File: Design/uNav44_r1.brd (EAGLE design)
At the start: 39.6 x 39.6 mm, 36 parts, among them IC1 DSPIC33FJ128MC, IC2 24LC024, Q1 10MHz

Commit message: Add 5 and 3.3V regulator / @katodo you must verify
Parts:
- removed PS: (no value), Personale:2POL254
- removed VR1: MCP1754S-3.3V, Personale:SOT89
- added C11, C13: 22uf, rcl:C1206
- added C12: 100nF/S, rcl:C0603
- added C14, C15: 10nF/S, rcl:C0603
- added IC3: (no value), OfficineRobotiche:SOT-23-5
- added IC4: (no value), OfficineRobotiche:SO-8EP
- added L2, L3: 22 uH, SparkFun-Passives:0805
- added PS1: (no value), Personale:2POL254
- added R10, R12: 10K0/S 1%, rcl:R0603
- added R11: 45K3/S 1%, rcl:R0603
- added R9: 100K0/S 1%, rcl:R0603
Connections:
- new net N$1: IC3.3, L3.1
- new net N$15: C14.2, IC4.3, L2.1
- new net N$16: C15.1, IC4.6
- new net N$17: C15.2, R12.2
- new net N$4: C14.1, IC4.1
- new net N$6: IC4.7, R9.1
- new net N$8: C12.1, IC4.8
- new net N$9: IC4.5, R10.1, R11.1
- net +12V: now also C11.1, IC4.2, PS1.2, R9.2
- net +3V3: now also IC3.5, L3.2; no longer VR1.3
- net +5V: now also C13.1, IC3.1, IC3.4, L2.2, R11.2; no longer PS.1, VR1.1
- net GND: now also C11.2, C12.2, C13.2, IC3.2, IC4.4, IC4.PAD, PS1.1, R10.2, R12.1; no longer PS.2, VR1.2, VR1.4
- net VENC: now also SJ3.2
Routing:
- net GND: track 279.7 -> 273.1 mm
- net +5V: track 61.7 -> 59.4 mm

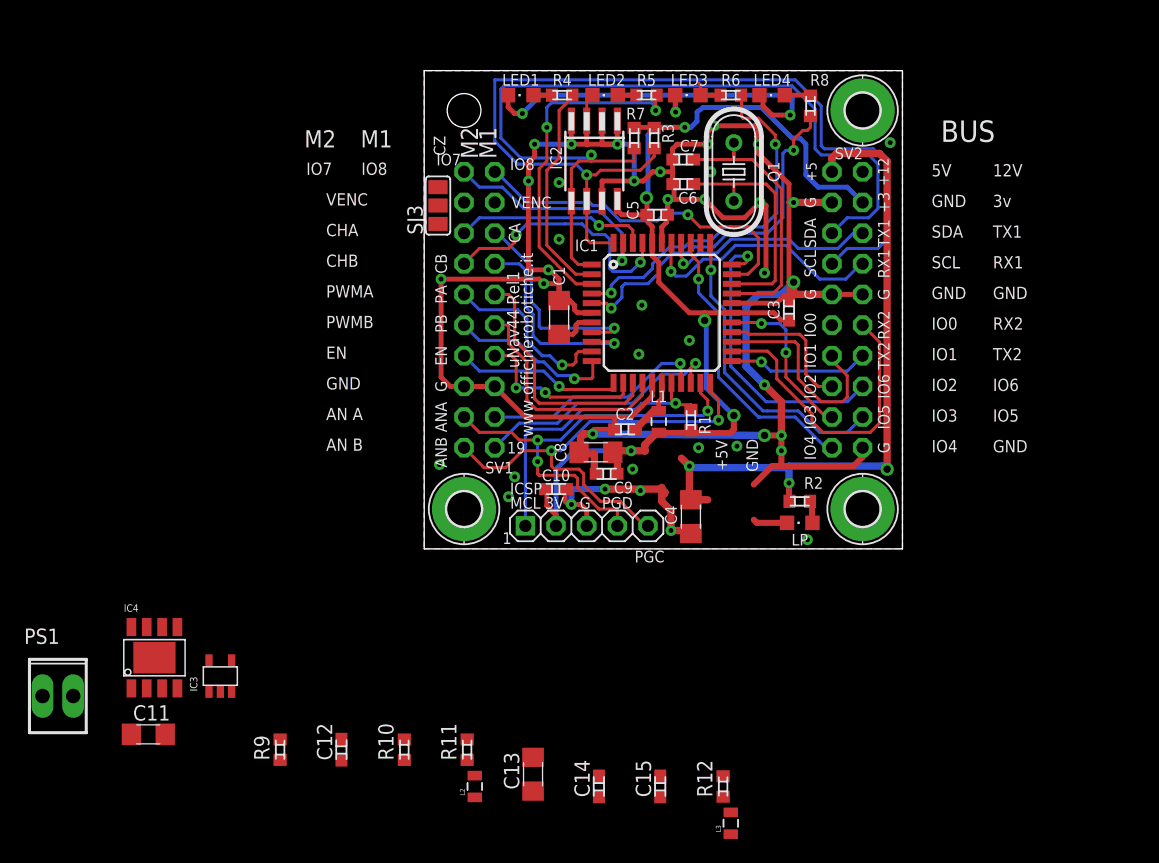
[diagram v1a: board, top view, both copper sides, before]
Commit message: Changed some component package to optimize space.
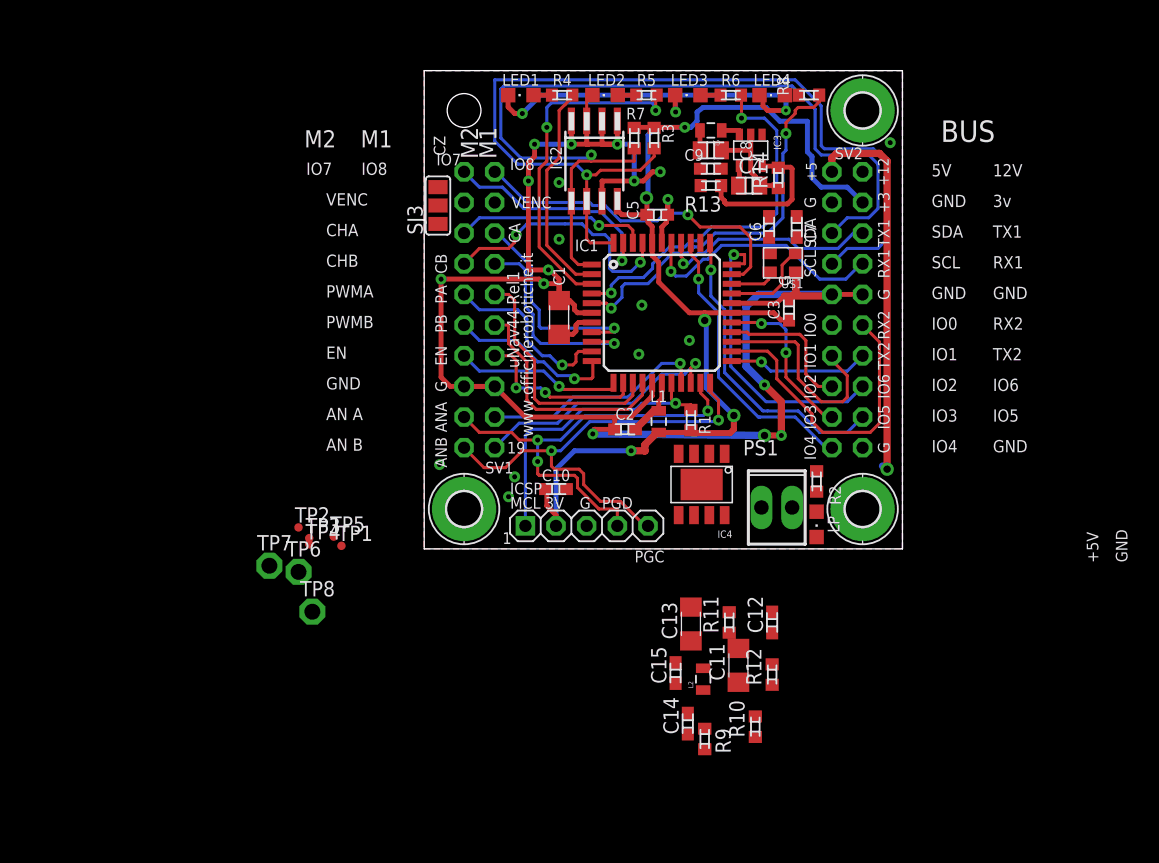
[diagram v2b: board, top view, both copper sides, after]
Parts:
- removed Q1: 10MHz, crystal:HC49U-V
- added R13: 450K/S 1%, rcl:R0603
- added R14: 100K/S 1%, rcl:R0603
- added TP1, TP2, TP3, TP4, TP5: PTR1TP07R, testpad:TP07R
- added TP6, TP7, TP8: PTR1PAD1-13, testpad:P1-13
- added U$1: CTS_32X25_SMD, cts_crystal:CTS_32X25
- C4, C8: value 22uf -> 10uF 10V X7R; device rcl:C1206 -> rcl:C0805
- IC3: value (none) -> AP3417CK-3.3TRG1
- IC4: value (none) -> AP6503SP-13
- L3: value 22 uH -> ASMPH-0805-2R2M-T
- moved IC3 61.9 mm to (23.7, 29.7), turned to 180 degrees
- moved PS1 61.6 mm to (25.9, 0.13)
- moved L3 57.4 mm to (20.4, 31.4), turned to 180 degrees
- moved C11 49.2 mm to (22.7, -13.0), turned to 90 degrees
- moved IC4 47.6 mm to (19.7, 2.03), turned to 180 degrees
- moved C12 37.2 mm to (25.5, -9.40)
- moved R9 35.2 mm to (19.9, -19.1), turned to 270 degrees
- moved R10 29.1 mm to (24.1, -18.0)
- moved C4 27.9 mm to (23.6, 26.8), turned to 0 degrees
- moved C8 26.8 mm to (20.4, 29.7), turned to 0 degrees
- moved C9 26.7 mm to (20.4, 28.2), turned to 0 degrees
- moved R11 24.1 mm to (22.0, -9.40)
- moved L2 20.9 mm to (19.8, -14.1)
- moved C13 18.1 mm to (18.8, -9.53)
- moved C7 10.9 mm to (27.6, 23.4), turned to 270 degrees
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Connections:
- new net N$7: IC3.5, R13.1, R14.2
- net +3V3: now also R13.2, TP1.TP; no longer IC3.5
- net +5V: now also TP2.TP
- net GND: now also R14.1, TP6.TP, TP7.TP, TP8.TP, U$1.2, U$1.4
- net N$2: now also U$1.1; no longer Q1.1
- net N$3: now also U$1.3; no longer Q1.2
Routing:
- net GND: track 273.1 -> 189.6 mm, vias 44 -> 26
- net +5V: track 59.4 -> 33.7 mm, vias 3 -> 1
- net N$2: track 23.4 -> 7.61 mm
- net N$3: track 19.4 -> 3.83 mm
- net N$7: track 0.00 -> 12.5 mm
- net VENC2-LD4: track 2.61 -> 0.35 mm
- net LD4: track 29.9 -> 32.1 mm
- net N$5: track 1.98 -> 0.00 mm
- net N$1: track 0.00 -> 1.81 mm
- net IO8: track 29.3 -> 28.2 mm
- net VENC1-LD3: track 2.74 -> 1.66 mm
- net +3V3: track 98.2 -> 97.2 mm
- net LD3: track 30.6 -> 31.1 mm

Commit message: Scheme update with Operational Amplifier and switching supply
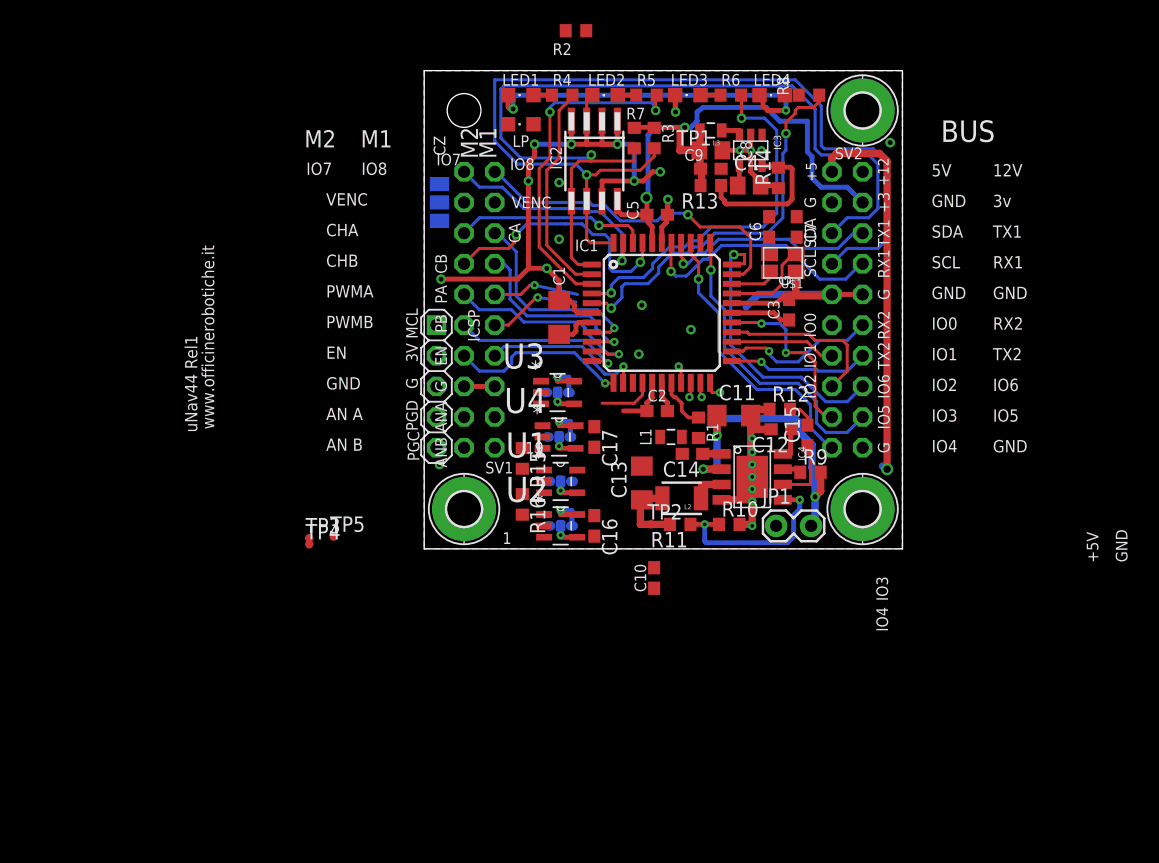
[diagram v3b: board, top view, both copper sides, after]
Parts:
- removed PS1: (no value), Personale:2POL254
- removed TP6, TP7, TP8: PTR1PAD1-13, testpad:P1-13
- added C16, C17: 100nF/S, rcl:C0603
- added JMP1, JMP2, JMP3, JMP4: 0R-JUMPC, jump-0r-smd:C0R-JMP
- added JP1: M02LOCK, SparkFun-Connectors:1X02_LOCK
- added R15, R16: 10K0/S 1%, rcl:R0603
- added U1, U2, U3, U4: MCP6G01T-E/OT, OfficineRobotiche:SOT95P300X145-5N
- C11: value 22uf -> 22uF 35V 20% JB 1206
- C12: value 100nF/S -> 100nF/S2
- C15: value 10nF/S -> 10nF/S2
- L2: value 22 uH -> 10uH_520mA; device SparkFun-Passives:0805 -> SparkFun-Passives:1210
- R9: value 100K0/S 1% -> 100K0/S2 1%
- U$1: value CTS_32X25_SMD -> (none); device cts_crystal:CTS_32X25 -> OfficineRobotiche:CTS_32X25
- moved TP1 43.1 mm to (17.9, 29.7)
- moved R2 42.3 mm to (9.27, 39.6), turned to 0 degrees
- moved LP 41.2 mm to (4.70, 31.9), turned to 90 degrees
- moved TP2 29.2 mm to (15.5, -1.27)
- moved R9 23.8 mm to (28.7, 3.05), turned to 0 degrees
- moved C15 22.5 mm to (28.4, 6.10)
- moved C14 22.4 mm to (18.9, 4.57), turned to 180 degrees
- moved R12 22.0 mm to (26.2, 8.26), turned to 0 degrees
- moved C11 20.7 mm to (22.4, 7.75), turned to 0 degrees
- moved ICSP 17.0 mm to (-2.29, 10.2), turned to 270 degrees
- moved R10 16.9 mm to (22.0, -1.27), turned to 0 degrees
- moved C12 16.0 mm to (26.3, 6.60), turned to 180 degrees
- moved L2 15.1 mm to (18.0, 0.89), turned to 180 degrees
- moved C13 12.4 mm to (14.7, 2.16)
- moved C10 11.0 mm to (15.7, -5.71), turned to 90 degrees
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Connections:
- new net ANA2/PGD: IC1.21, ICSP.4, R15.1
- new net ANB2/PGC: IC1.22, ICSP.5, R16.1
- new net IN_A1: SV1.17, U3.3
- new net IN_B1: SV1.19, U4.3
- new net N$11: JMP1.2, U1.4
- new net N$18: JMP2.2, U2.4
- new net N$19: JMP3.2, U3.4
- new net N$20: JMP4.2, U4.4
- new net N$21: R15.2, U1.1
- new net N$22: R16.2, U2.1
- net +12V: now also JP1.2; no longer PS1.2
- net +3V3: now also C16.1, C17.1, JMP1.1, JMP2.1, JMP3.1, JMP4.1, U1.5, U2.5, U3.5, U4.5
- net ANA1: now also U3.1; no longer SV1.17
- net ANA2: now also U1.3; no longer IC1.21, ICSP.4
- net ANB1: now also U4.1; no longer SV1.19
- net ANB2: now also U2.3; no longer IC1.22, ICSP.5
- net GND: now also C16.2, C17.2, JMP1.3, JMP2.3, JMP3.3, JMP4.3, JP1.1, U1.2, U2.2, U3.2, U4.2; no longer PS1.1, TP6.TP, TP7.TP, TP8.TP
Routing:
- net ANB2: track 38.7 -> 0.00 mm, vias 2 -> 0
- net ANA2: track 37.0 -> 0.00 mm, vias 3 -> 0
- net GND: track 189.6 -> 153.3 mm, vias 26 -> 29
- net +3V3: track 97.2 -> 70.2 mm
- net +12V: track 0.00 -> 26.7 mm, vias 0 -> 3
- net MCLR: track 24.6 -> 4.38 mm, vias 1 -> 0
- net ANB1: track 21.3 -> 1.29 mm
- net ANA1: track 18.8 -> 1.44 mm
- net N$9: track 0.00 -> 16.0 mm, vias 0 -> 2
- net PWMA1: track 20.3 -> 7.25 mm, vias 0 -> 1
- net RX2: track 25.3 -> 12.9 mm, vias 0 -> 1
- net IO1: track 17.4 -> 8.78 mm
- net PWMB1: track 19.4 -> 12.3 mm, vias 0 -> 1
- net +5V: track 33.7 -> 40.1 mm
- net N$16: track 0.00 -> 5.75 mm
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
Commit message: Work in progress... update image of layout
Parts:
- added C18, C19: 100nF/S, rcl:C0603
- moved C10 23.7 mm to (4.95, 15.4)
- moved R2 13.1 mm to (0.13, 30.2), turned to 180 degrees
- moved C6 3.29 mm to (23.7, 20.4)
- moved JMP3 2.07 mm to (6.22, 11.0)
- moved U3 2.07 mm to (6.22, 11.0)
- moved C7 1.55 mm to (26.3, 22.5), turned to 0 degrees
- moved TP2 1.53 mm to (14.0, -1.40)
- moved L1 1.31 mm to (16.0, 6.60), turned to 180 degrees
- moved R11 1.14 mm to (17.9, -2.41)
- moved L3 0.89 mm to (20.4, 32.3)
- moved C13 0.76 mm to (14.0, 2.16)
- moved C4 0.51 mm to (23.6, 26.3)
- moved TP1 0.51 mm to (17.4, 29.7)
- moved R14 0.40 mm to (26.2, 27.1)
- moved C5 0.38 mm to (16.0, 24.8)
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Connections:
- net +3V3: now also C18.1, C19.1
- net GND: now also C18.2, C19.2
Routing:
- net +3V3: track 70.2 -> 151.4 mm, vias 5 -> 10
- net GND: track 153.3 -> 233.2 mm, vias 29 -> 38
- net +5V: track 40.1 -> 117.2 mm, vias 1 -> 6
- net ANB2/PGC: track 1.52 -> 37.9 mm, vias 1 -> 4
- net +12V: track 26.7 -> 57.7 mm, vias 3 -> 4
- net ANA2/PGD: track 1.27 -> 29.0 mm, vias 1 -> 2
- net ANA1: track 1.44 -> 20.7 mm, vias 1 -> 2
- net ANB1: track 1.29 -> 18.8 mm, vias 1 -> 2
- net MCLR: track 4.38 -> 21.2 mm
- net ANB2: track 0.00 -> 12.5 mm
- net ANA2: track 0.00 -> 12.2 mm, vias 0 -> 2
- net PWMA1: track 7.25 -> 17.8 mm, vias 1 -> 2
- net N$5: track 0.00 -> 6.18 mm
- net IN_B1: track 0.00 -> 5.27 mm
- net PWMB1: track 12.3 -> 16.9 mm
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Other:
- board size 39.6 x 39.6 mm -> 39.9 x 39.9 mm

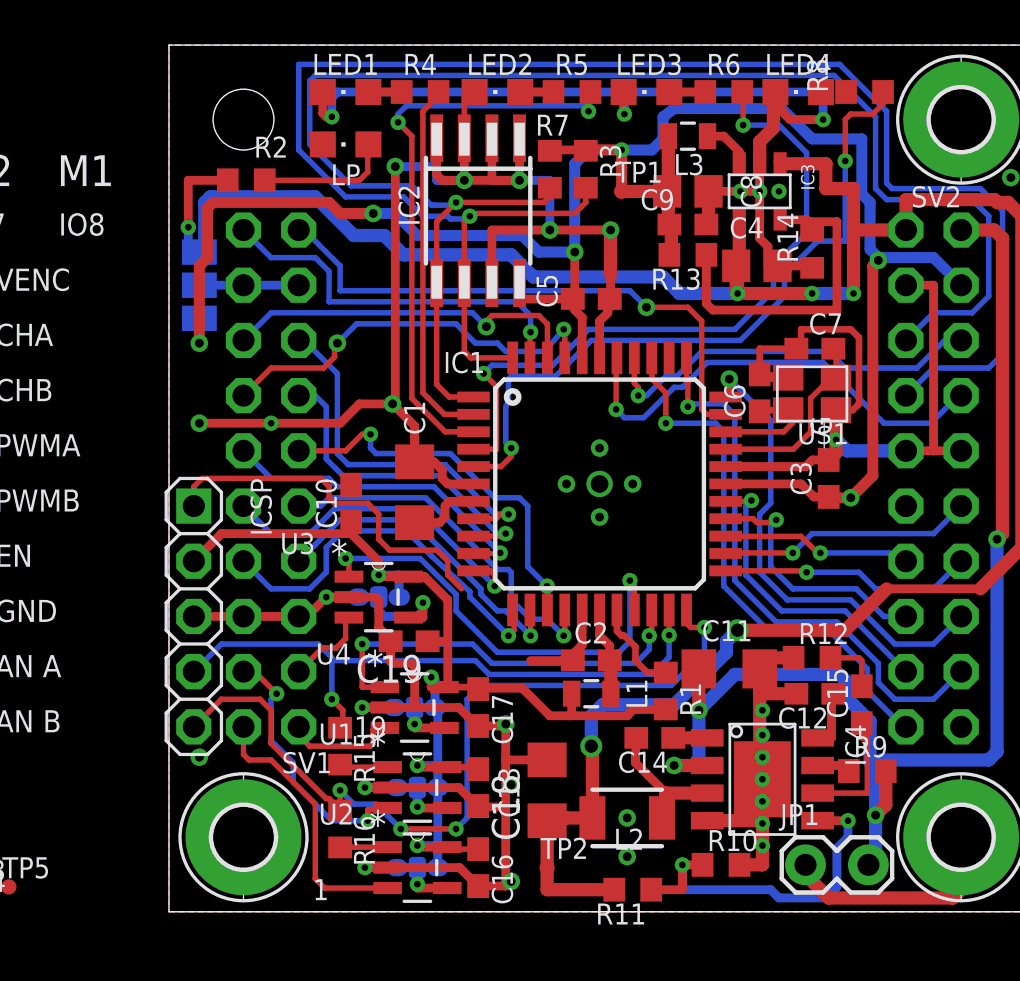
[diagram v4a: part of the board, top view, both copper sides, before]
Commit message: Re-Added LDO regulator as option for a LOW-COST version of board. Added jumper to fix IO7 & IO8 to GND to facilitate Encoder cabling in application without Z-Axis
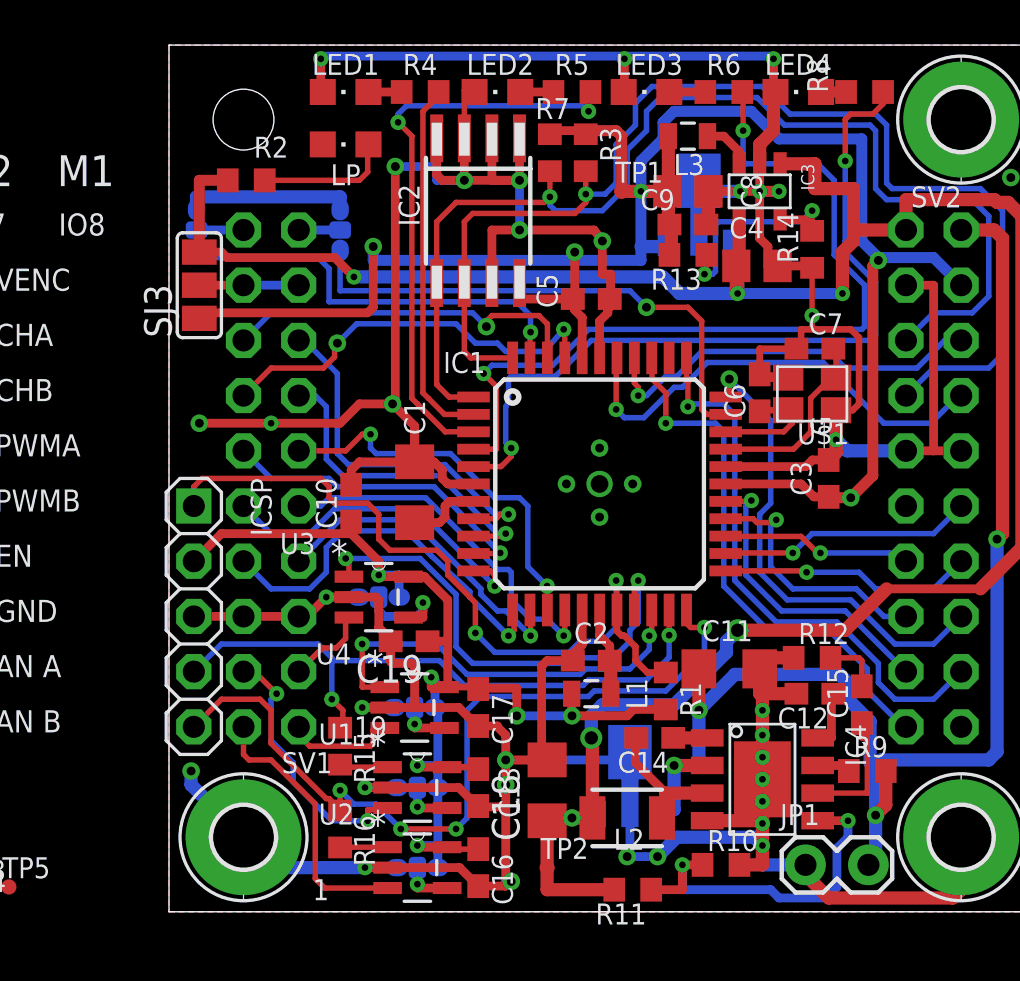
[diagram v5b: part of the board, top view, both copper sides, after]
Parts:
- added JMP5, JMP6: 0R-JUMPC, jump-0r-smd:C0R-JMP
- added VR1: MCP1754S-3.3V, Personale:SOT89
- added VR2: MCP1754S-5.0V, Personale:SOT89
- moved R3 0.76 mm to (15.7, 31.5)
- moved R7 0.76 mm to (14.1, 31.5)
- flipped SJ3 to the top
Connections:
- new net N$10: JMP5.2, SV1.2
- new net N$23: JMP6.2, SV1.1
- net +12V: now also VR2.1
- net +3V3: now also VR1.3
- net +5V: now also VR1.1, VR2.3
- net GND: now also JMP5.3, JMP6.3, VR1.2, VR1.4, VR2.2, VR2.4
- net IO7: now also JMP5.1; no longer SV1.2
- net IO8: now also JMP6.1; no longer SV1.1
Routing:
- net GND: track 233.2 -> 281.5 mm, vias 38 -> 39
- net SCL: track 77.1 -> 54.3 mm
- net SDA: track 70.7 -> 52.8 mm
- net MCLR: track 21.2 -> 34.3 mm, vias 0 -> 2
- net LD3: track 31.8 -> 38.4 mm
- net N$7: track 15.9 -> 11.1 mm, vias 0 -> 2
- net LD4: track 32.5 -> 36.4 mm
- net +12V: track 57.7 -> 60.4 mm
- net N$10: track 0.00 -> 2.16 mm
- net N$23: track 0.00 -> 1.91 mm
- net IO8: track 26.2 -> 24.3 mm
- net IO7: track 17.6 -> 19.5 mm
- net ANA1: track 20.7 -> 22.2 mm
- net VENC2-LD4: track 0.35 -> 1.50 mm
- net +5V: track 117.2 -> 116.3 mm
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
